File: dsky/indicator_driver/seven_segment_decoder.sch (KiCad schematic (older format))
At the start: 25 parts, among them K1 EC2-12TNU, K2 EC2-12TNU, K3 EC2-12TNU, K4 EC2-12TNU, K5 EC2-12TNU

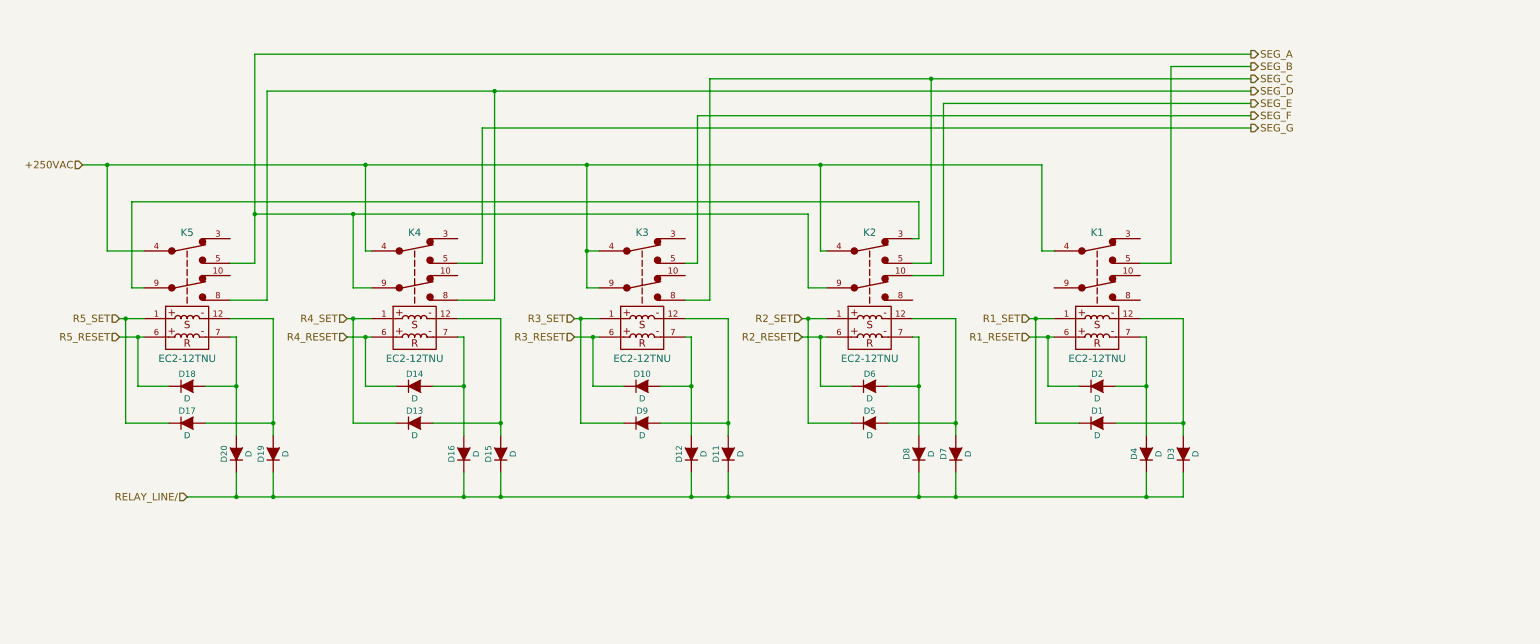
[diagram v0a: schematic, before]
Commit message: New (original) seven-segment decoder, taken from the Apollo 12 Mission Report
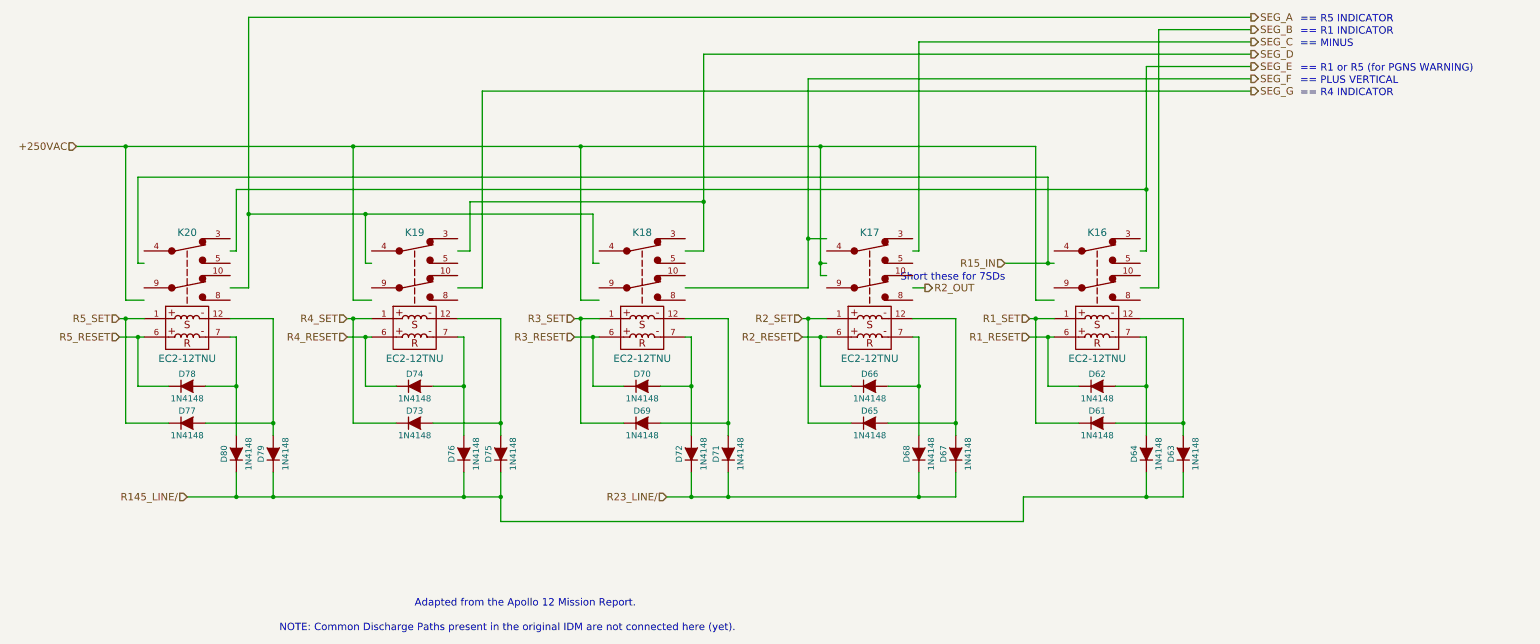
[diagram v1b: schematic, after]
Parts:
- D1, D10, D11, D12, D13, D14, D15, D16, D17, D18, D19, D2, D20, D3, D4, D5, D6, D7, D8, D9: value D -> 1N4148
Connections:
- net labels added: R145_LINE/, R15_IN, R23_LINE/, R2_OUT
- net labels removed: RELAY_LINE/
- wire segments 118 -> 126
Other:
- note added: "== MINUS"
- note added: "== PLUS VERTICAL"
- note added: "== R1 INDICATOR"
- note added: "== R1 or R5 (for PGNS WARNING)"
- note added: "== R4 INDICATOR"
- note added: "== R5 INDICATOR"
- note added: "Adapted from the Apollo 12 Mission Report."
- note added: "NOTE: Common Discharge Paths present in the original IDM are not connected here (yet)."
- note added: "Short these for 7SDs"

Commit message: Added in the rest of the IDM hardware. Values and diode matrix design still need to be finalized. Working on wiring everything up now.
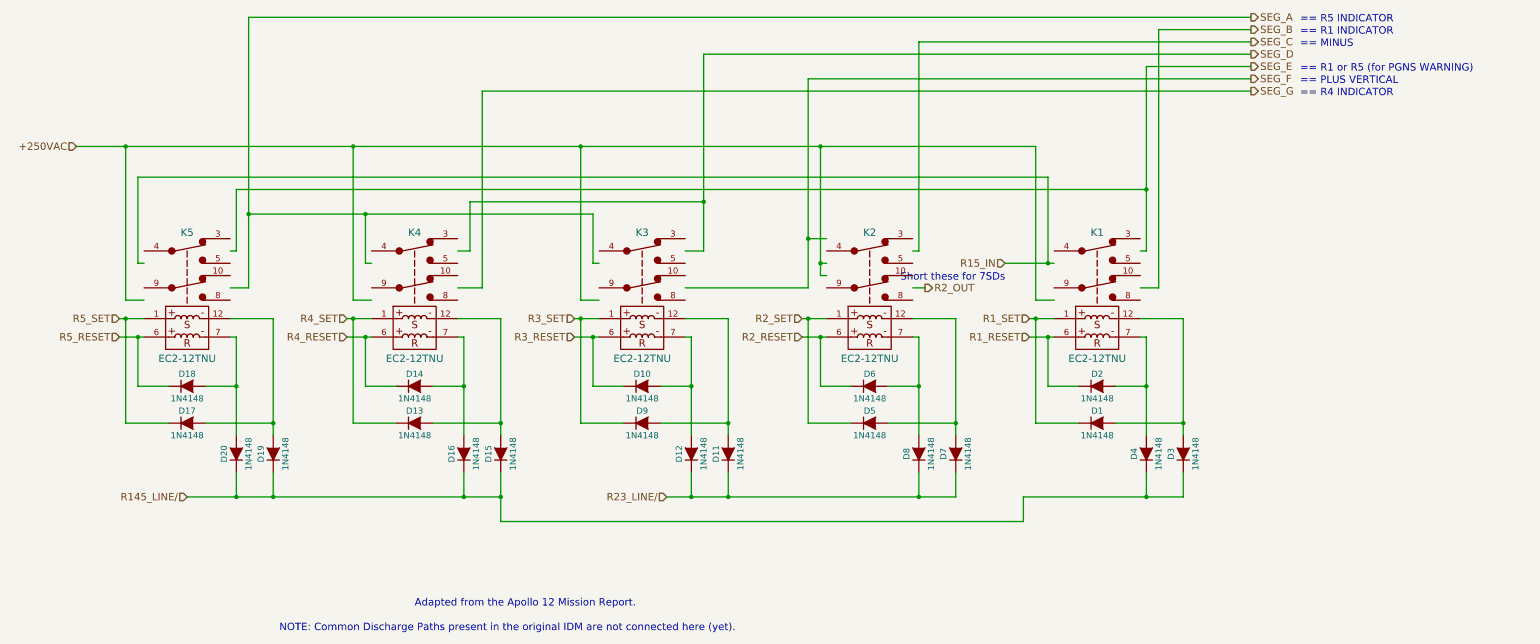
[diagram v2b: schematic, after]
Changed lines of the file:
@@
 $Descr A3 16535 11693
 encoding utf-8
-Sheet 5 5
+Sheet 2 12
 Title ""
 Date ""
@@
 AR Path="/582563A0/5736A05D" Ref="K15"  Part="1"
 AR Path="/582563BD/5736A05D" Ref="K20"  Part="1"
-F 0 "K20" H 3700 5750 60  0000 C CNN
+F 0 "K5" H 3700 5750 60  0000 C CNN
 F 1 "EC2-12TNU" H 3700 4725 60  0000 C CNN
 F 2 "" H 3700 5300 60  0000 C CNN
@@
 AR Path="/582563A0/5736B487" Ref="K13"  Part="1"
 AR Path="/582563BD/5736B487" Ref="K18"  Part="1"
-F 0 "K18" H 7400 5750 60  0000 C CNN
+F 0 "K3" H 7400 5750 60  0000 C CNN
 F 1 "EC2-12TNU" H 7400 4725 60  0000 C CNN
 F 2 "" H 7400 5300 60  0000 C CNN
@@
 AR Path="/582563A0/5736B4D2" Ref="K12"  Part="1"
 AR Path="/582563BD/5736B4D2" Ref="K17"  Part="1"
-F 0 "K17" H 9250 5750 60  0000 C CNN
+F 0 "K2" H 9250 5750 60  0000 C CNN
 F 1 "EC2-12TNU" H 9250 4725 60  0000 C CNN
 F 2 "" H 9250 5300 60  0000 C CNN
@@
 AR Path="/582563A0/5736B58C" Ref="K11"  Part="1"
 AR Path="/582563BD/5736B58C" Ref="K16"  Part="1"
-F 0 "K16" H 11100 5750 60  0000 C CNN
+F 0 "K1" H 11100 5750 60  0000 C CNN
 F 1 "EC2-12TNU" H 11100 4725 60  0000 C CNN
 F 2 "" H 11100 5300 60  0000 C CNN
@@
 AR Path="/582563A0/5736D2BE" Ref="D59"  Part="1"
 AR Path="/582563BD/5736D2BE" Ref="D79"  Part="1"
-F 0 "D79" H 4400 6850 50  0000 C CNN
+F 0 "D19" H 4400 6850 50  0000 C CNN
 F 1 "1N4148" H 4400 6650 50  0000 C CNN
 F 2 "" H 4400 6750 60  0000 C CNN
@@
 AR Path="/582563A0/5736D4D2" Ref="D60"  Part="1"
 AR Path="/582563BD/5736D4D2" Ref="D80"  Part="1"
-F 0 "D80" H 4100 6850 50  0000 C CNN
+F 0 "D20" H 4100 6850 50  0000 C CNN
 F 1 "1N4148" H 4100 6650 50  0000 C CNN
 F 2 "" H 4100 6750 60  0000 C CNN
@@
 AR Path="/582563A0/5736EB71" Ref="D56"  Part="1"
 AR Path="/582563BD/5736EB71" Ref="D76"  Part="1"
-F 0 "D76" H 5950 6850 50  0000 C CNN
+F 0 "D16" H 5950 6850 50  0000 C CNN
 F 1 "1N4148" H 5950 6650 50  0000 C CNN
 F 2 "" H 5950 6750 60  0000 C CNN
@@
 AR Path="/582563A0/5736EB77" Ref="D55"  Part="1"
 AR Path="/582563BD/5736EB77" Ref="D75"  Part="1"
-F 0 "D75" H 6250 6850 50  0000 C CNN
+F 0 "D15" H 6250 6850 50  0000 C CNN
 F 1 "1N4148" H 6250 6650 50  0000 C CNN
 F 2 "" H 6250 6750 60  0000 C CNN
@@
 AR Path="/582563A0/5736F1E0" Ref="D52"  Part="1"
 AR Path="/582563BD/5736F1E0" Ref="D72"  Part="1"
-F 0 "D72" H 7800 6850 50  0000 C CNN
+F 0 "D12" H 7800 6850 50  0000 C CNN
 F 1 "1N4148" H 7800 6650 50  0000 C CNN
 F 2 "" H 7800 6750 60  0000 C CNN
@@
 AR Path="/582563A0/5736F1E6" Ref="D51"  Part="1"
 AR Path="/582563BD/5736F1E6" Ref="D71"  Part="1"
-F 0 "D71" H 8100 6850 50  0000 C CNN
+F 0 "D11" H 8100 6850 50  0000 C CNN
 F 1 "1N4148" H 8100 6650 50  0000 C CNN
 F 2 "" H 8100 6750 60  0000 C CNN
@@
 AR Path="/582563A0/5736F3A7" Ref="D48"  Part="1"
 AR Path="/582563BD/5736F3A7" Ref="D68"  Part="1"
-F 0 "D68" H 9650 6850 50  0000 C CNN
+F 0 "D8" H 9650 6850 50  0000 C CNN
 F 1 "1N4148" H 9650 6650 50  0000 C CNN
 F 2 "" H 9650 6750 60  0000 C CNN
@@
 AR Path="/582563A0/5736F3AD" Ref="D47"  Part="1"
 AR Path="/582563BD/5736F3AD" Ref="D67"  Part="1"
-F 0 "D67" H 9950 6850 50  0000 C CNN
+F 0 "D7" H 9950 6850 50  0000 C CNN
 F 1 "1N4148" H 9950 6650 50  0000 C CNN
 F 2 "" H 9950 6750 60  0000 C CNN
@@
 AR Path="/582563A0/5736FBD9" Ref="D44"  Part="1"
 AR Path="/582563BD/5736FBD9" Ref="D64"  Part="1"
-F 0 "D64" H 11500 6850 50  0000 C CNN
+F 0 "D4" H 11500 6850 50  0000 C CNN
 F 1 "1N4148" H 11500 6650 50  0000 C CNN
 F 2 "" H 11500 6750 60  0000 C CNN
@@
 AR Path="/582563A0/5736FBDF" Ref="D43"  Part="1"
 AR Path="/582563BD/5736FBDF" Ref="D63"  Part="1"
-F 0 "D63" H 11800 6850 50  0000 C CNN
+F 0 "D3" H 11800 6850 50  0000 C CNN
 F 1 "1N4148" H 11800 6650 50  0000 C CNN
 F 2 "" H 11800 6750 60  0000 C CNN
@@
 AR Path="/582563A0/5738D2AC" Ref="D58"  Part="1"
 AR Path="/582563BD/5738D2AC" Ref="D78"  Part="1"
-F 0 "D78" H 3700 6300 50  0000 C CNN
+F 0 "D18" H 3700 6300 50  0000 C CNN
 F 1 "1N4148" H 3700 6100 50  0000 C CNN
 F 2 "" H 3700 6200 60  0000 C CNN
@@
 AR Path="/582563A0/5738EBF5" Ref="D57"  Part="1"
 AR Path="/582563BD/5738EBF5" Ref="D77"  Part="1"
-F 0 "D77" H 3700 6600 50  0000 C CNN
+F 0 "D17" H 3700 6600 50  0000 C CNN
 F 1 "1N4148" H 3700 6400 50  0000 C CNN
 F 2 "" H 3700 6500 60  0000 C CNN
@@
 AR Path="/582563A0/573934E1" Ref="D54"  Part="1"
 AR Path="/582563BD/573934E1" Ref="D74"  Part="1"
-F 0 "D74" H 5550 6300 50  0000 C CNN
+F 0 "D14" H 5550 6300 50  0000 C CNN
 F 1 "1N4148" H 5550 6100 50  0000 C CNN
 F 2 "" H 5550 6200 60  0000 C CNN
@@
 AR Path="/582563A0/573934E7" Ref="D53"  Part="1"
 AR Path="/582563BD/573934E7" Ref="D73"  Part="1"
-F 0 "D73" H 5550 6600 50  0000 C CNN
+F 0 "D13" H 5550 6600 50  0000 C CNN
 F 1 "1N4148" H 5550 6400 50  0000 C CNN
 F 2 "" H 5550 6500 60  0000 C CNN
@@
 AR Path="/582563A0/57394E76" Ref="D50"  Part="1"
 AR Path="/582563BD/57394E76" Ref="D70"  Part="1"
-F 0 "D70" H 7400 6300 50  0000 C CNN
+F 0 "D10" H 7400 6300 50  0000 C CNN
 F 1 "1N4148" H 7400 6100 50  0000 C CNN
 F 2 "" H 7400 6200 60  0000 C CNN
@@
 AR Path="/582563A0/57394E7C" Ref="D49"  Part="1"
 AR Path="/582563BD/57394E7C" Ref="D69"  Part="1"
-F 0 "D69" H 7400 6600 50  0000 C CNN
+F 0 "D9" H 7400 6600 50  0000 C CNN
 F 1 "1N4148" H 7400 6400 50  0000 C CNN
 F 2 "" H 7400 6500 60  0000 C CNN
@@
 AR Path="/582563A0/5739DEC3" Ref="D46"  Part="1"
 AR Path="/582563BD/5739DEC3" Ref="D66"  Part="1"
-F 0 "D66" H 9250 6300 50  0000 C CNN
+F 0 "D6" H 9250 6300 50  0000 C CNN
 F 1 "1N4148" H 9250 6100 50  0000 C CNN
 F 2 "" H 9250 6200 60  0000 C CNN
@@
 AR Path="/582563A0/5739DEC9" Ref="D45"  Part="1"
 AR Path="/582563BD/5739DEC9" Ref="D65"  Part="1"
-F 0 "D65" H 9250 6600 50  0000 C CNN
+F 0 "D5" H 9250 6600 50  0000 C CNN
 F 1 "1N4148" H 9250 6400 50  0000 C CNN
 F 2 "" H 9250 6500 60  0000 C CNN
@@
 AR Path="/582563A0/573A3828" Ref="D42"  Part="1"
 AR Path="/582563BD/573A3828" Ref="D62"  Part="1"
-F 0 "D62" H 11100 6300 50  0000 C CNN
+F 0 "D2" H 11100 6300 50  0000 C CNN
 F 1 "1N4148" H 11100 6100 50  0000 C CNN
 F 2 "" H 11100 6200 60  0000 C CNN
@@
 AR Path="/582563A0/573A382E" Ref="D41"  Part="1"
 AR Path="/582563BD/573A382E" Ref="D61"  Part="1"
-F 0 "D61" H 11100 6600 50  0000 C CNN
+F 0 "D1" H 11100 6600 50  0000 C CNN
 F 1 "1N4148" H 11100 6400 50  0000 C CNN
 F 2 "" H 11100 6500 60  0000 C CNN
@@
 AR Path="/582563A0/5736B3D3" Ref="K14"  Part="1"
 AR Path="/582563BD/5736B3D3" Ref="K19"  Part="1"
-F 0 "K19" H 5550 5750 60  0000 C CNN
+F 0 "K4" H 5550 5750 60  0000 C CNN
 F 1 "EC2-12TNU" H 5550 4725 60  0000 C CNN
 F 2 "" H 5550 5300 60  0000 C CNN

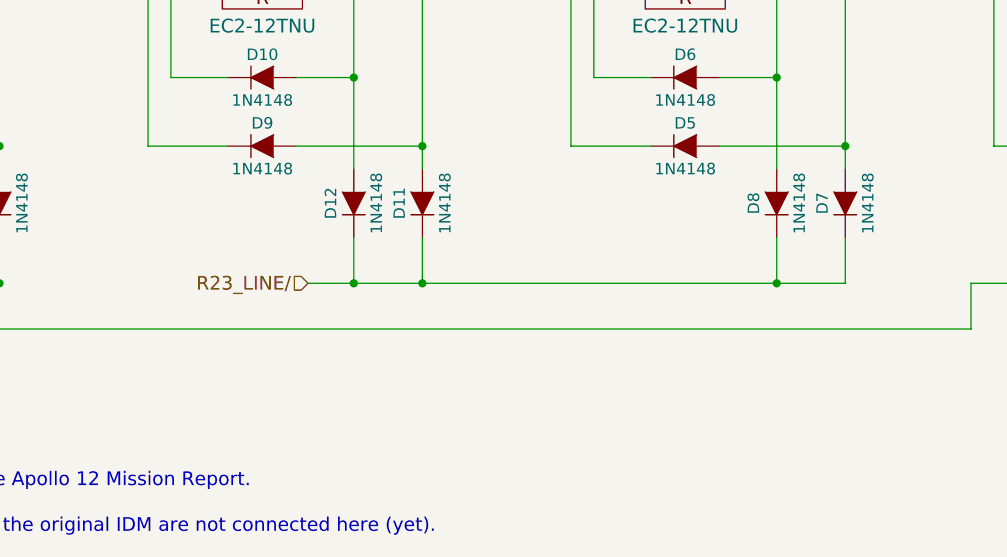
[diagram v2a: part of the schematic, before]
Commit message: Finished initial wiring of the Indicator Driver Module. Currently sitting at 111 pins used, so I've been too aggressive at culling pins
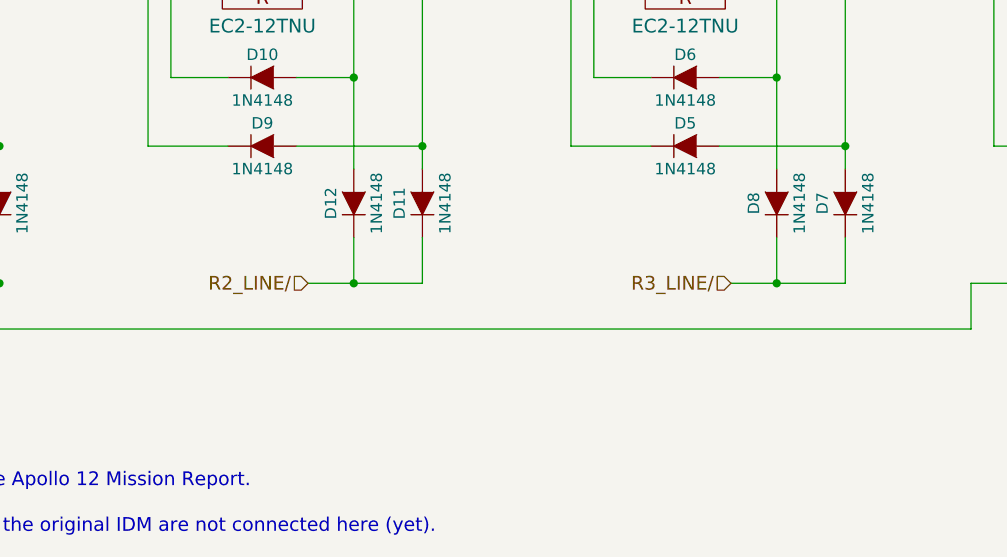
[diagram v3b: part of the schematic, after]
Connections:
- net labels added: R2_LINE/, R3_LINE/
- net labels removed: R23_LINE/
- wire segments 126 -> 127
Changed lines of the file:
@@
 	8100 7100 8100 6900
 Connection ~ 7800 7100
-Connection ~ 8100 7100
 $Comp
 L D D8
@@
 	10500 7100 11800 7100
 Text HLabel 7600 7100 0    60   Input ~ 0
-R23_LINE/
-Wire Wire Line
-	7600 7100 9950 7100
+R2_LINE/
 Wire Wire Line
 	3700 7100 6250 7100
@@
 Text Notes 12750 3350 0    60   ~ 0
 == R1 INDICATOR
+Wire Wire Line
+	8100 7100 7600 7100
+Text HLabel 9450 7100 0    60   Input ~ 0
+R3_LINE/
+Wire Wire Line
+	9950 7100 9450 7100
 $EndSCHEMATC

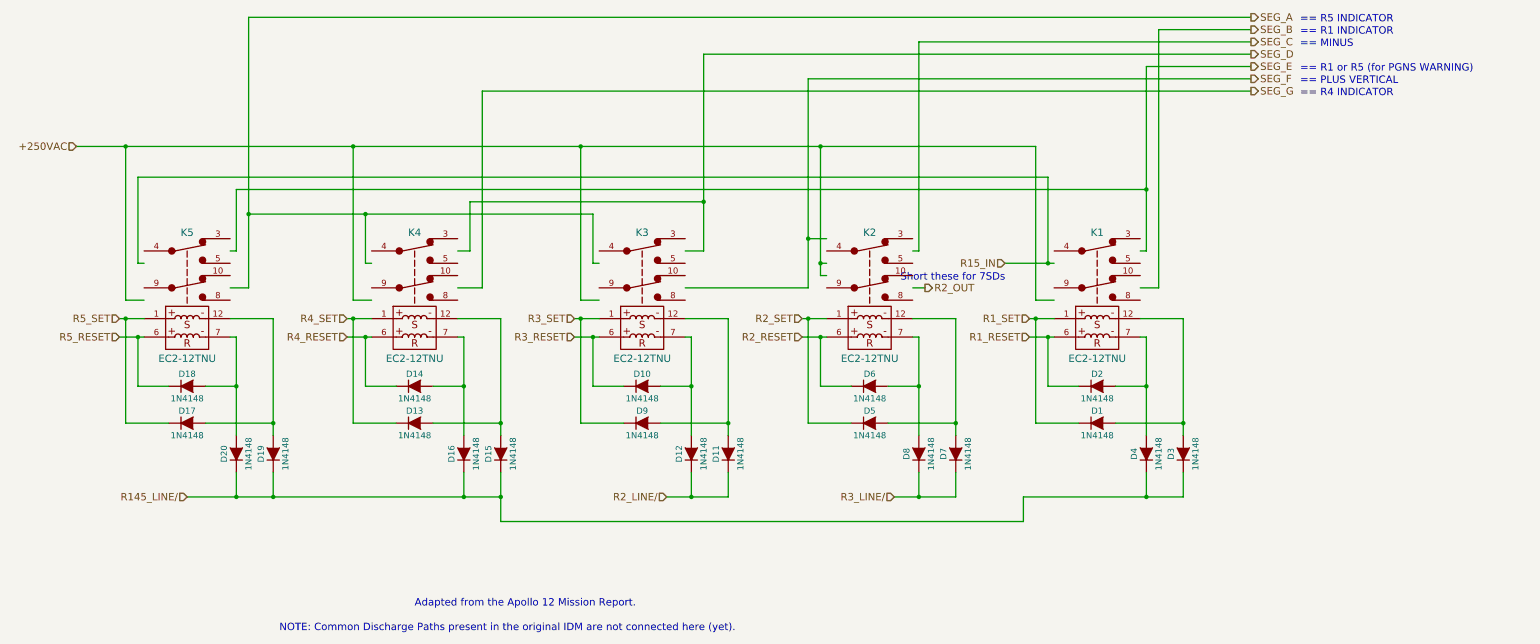
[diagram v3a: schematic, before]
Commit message: DSKY IDM: Cleaned up design rule errors. Still don't fully understand the common returh path.
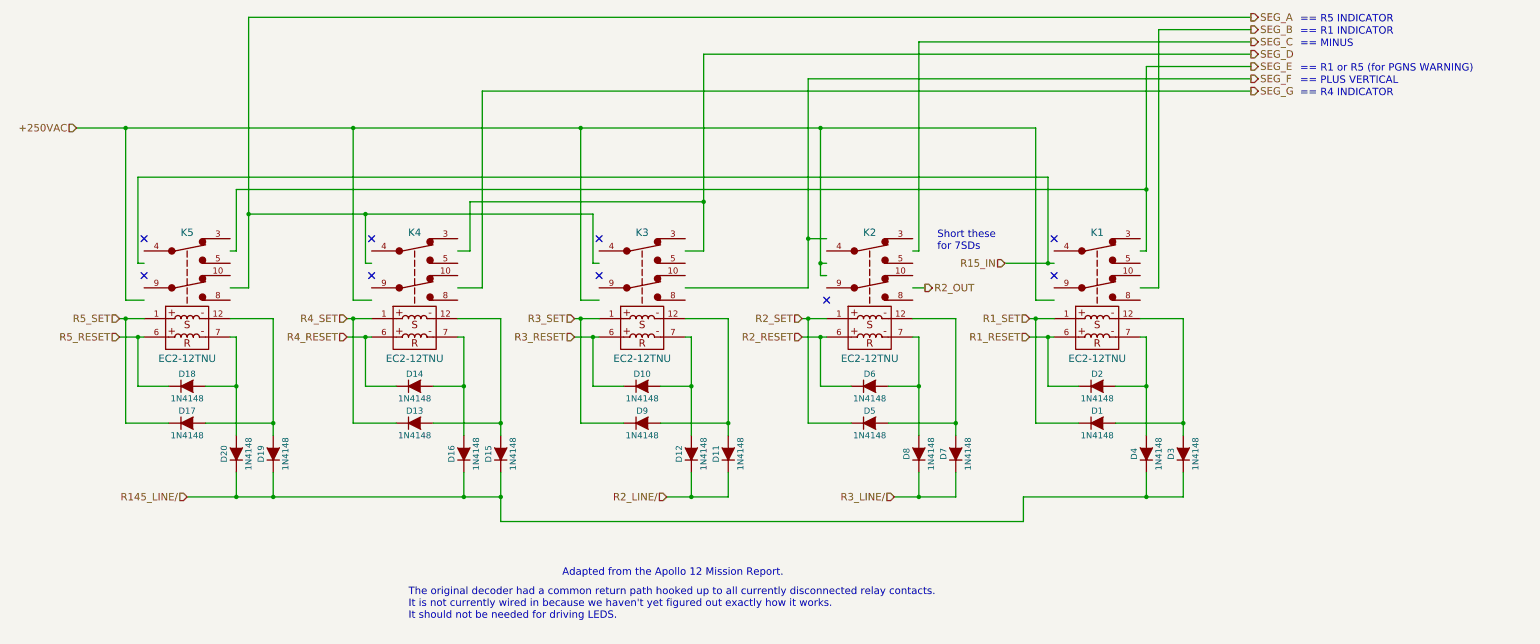
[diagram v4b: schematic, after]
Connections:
- no-connect marks 0 -> 9
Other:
- note added: "Short these \nfor 7SDs"
- note added: "The original decoder had a common return path hooked up to all currently disconnected relay contacts.\nIt is not currently wired in because we haven't yet figured out exactly how it works. \nIt should not be needed for driving LEDS."
- note removed: "NOTE: Common Discharge Paths present in the original IDM are not connected here (yet)."
- note removed: "Short these for 7SDs"
